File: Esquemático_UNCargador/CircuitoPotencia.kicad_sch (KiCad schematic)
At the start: 2 parts, among them J2 Neutro, J3 Conn_02x03_Counter_Clockwise

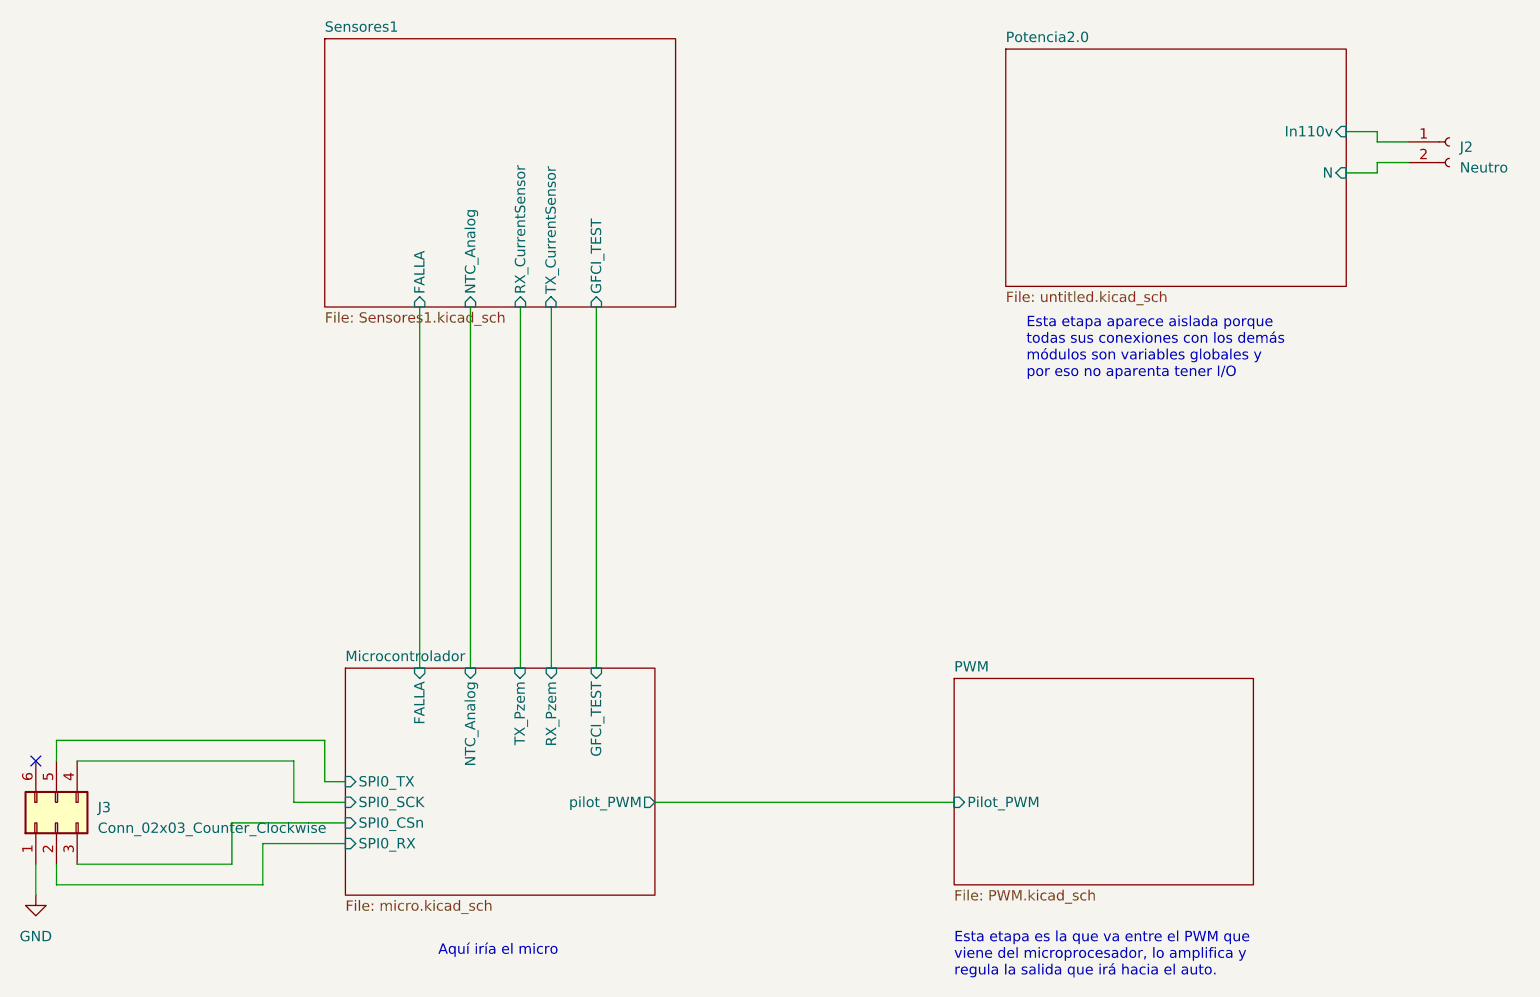
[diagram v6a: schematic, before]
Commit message: PCB con ruteo realizado. Errores en los anchos de vias -0.2mm. Huella LF356n actualizada
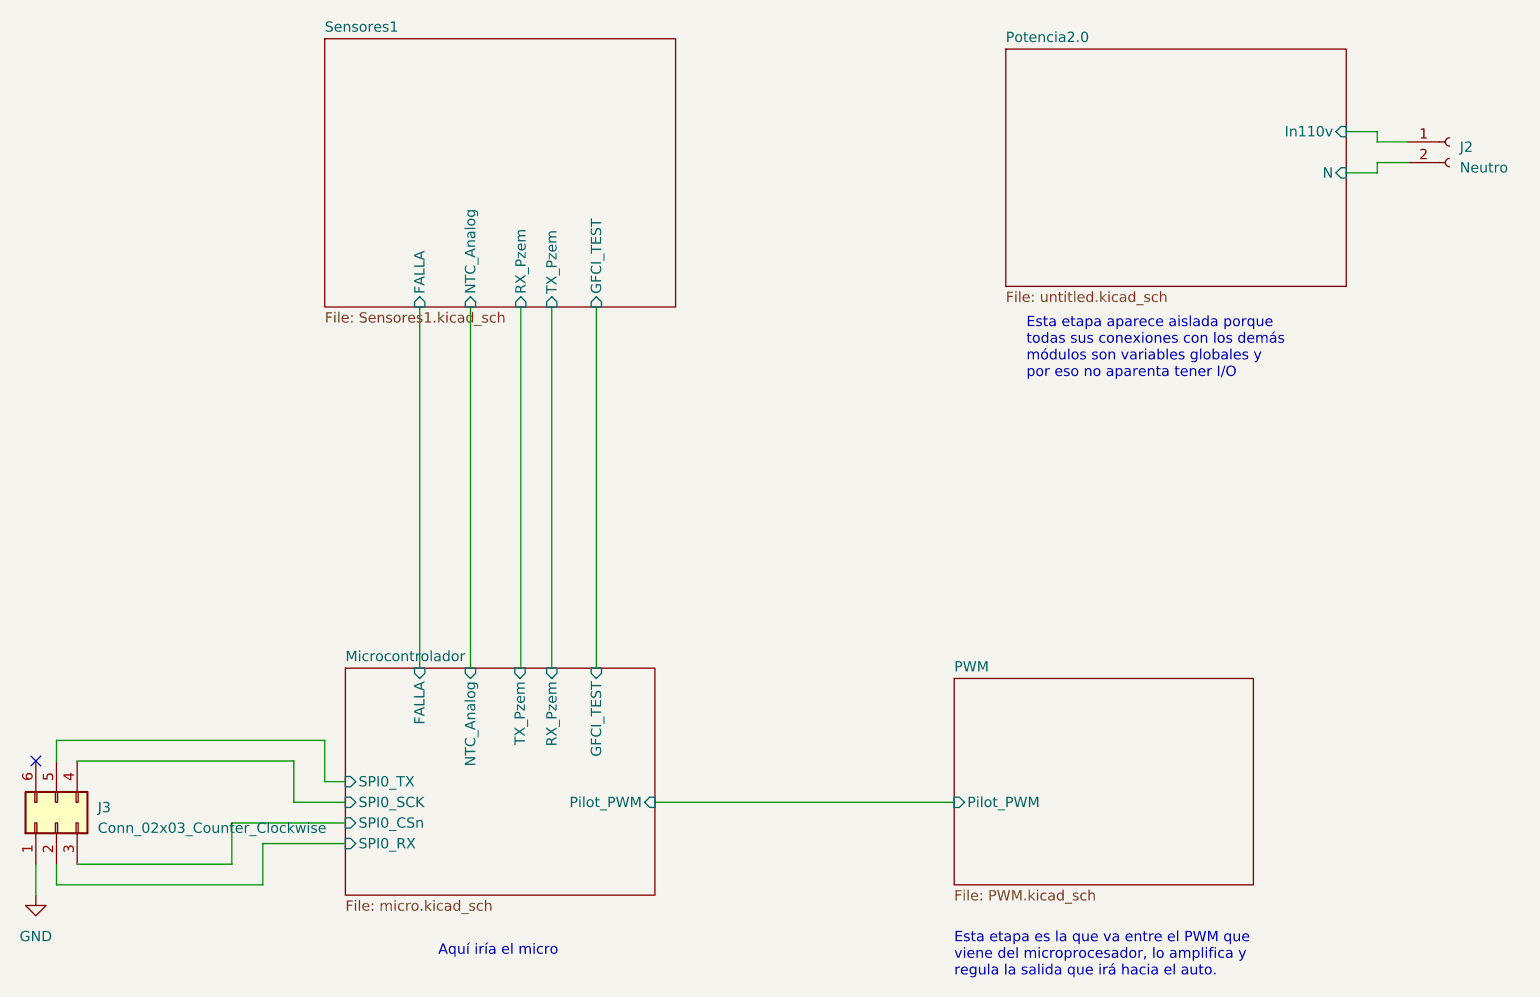
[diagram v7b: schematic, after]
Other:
- sheet Microcontrolador ports: added Pilot_PWM; removed pilot_PWM
- sheet Sensores1 ports: added RX_Pzem, TX_Pzem; removed RX_CurrentSensor, TX_CurrentSensor
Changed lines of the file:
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@@
   (paper "A4")
   (no_connect (at 20.32 129.54))
+  (wire (pts (xy 80.01 73.66) (xy 80.01 118.11))
+    (stroke (width 0) (type default))
+  )
   (wire (pts (xy 48.26 139.7) (xy 58.42 139.7))
     (stroke (width 0) (type default))
@@
     (stroke (width 0) (type default))
   )
+  (wire (pts (xy 83.82 73.66) (xy 83.82 118.11))
+    (stroke (width 0) (type default))
+  )
   (wire (pts (xy 22.86 129.54) (xy 22.86 127))
     (stroke (width 0) (type default))
@@
     (stroke (width 0) (type default))
   )
-  (wire (pts (xy 79.9592 73.66) (xy 79.9592 118.11))
-    (stroke (width 0) (type default))
-  )
   (wire (pts (xy 185.42 57.15) (xy 181.61 57.15))
     (stroke (width 0) (type default))
   )
-  (wire (pts (xy 83.7692 73.66) (xy 83.7692 118.11))
-    (stroke (width 0) (type default))
-  )
   (wire (pts (xy 52.07 129.54) (xy 25.4 129.54))
     (stroke (width 0) (type default))
@@
     (stroke (width 0) (type default))
   )
-  (wire (pts (xy 83.7692 73.66) (xy 83.7184 73.66))
-    (stroke (width 0) (type default))
-  )
   (wire (pts (xy 185.42 52.07) (xy 181.61 52.07))
     (stroke (width 0) (type default))
@@
     (stroke (width 0) (type default))
   )
-  (wire (pts (xy 79.9592 118.11) (xy 79.9084 118.11))
+  (wire (pts (xy 80.01 118.11) (xy 79.9084 118.11))
     (stroke (width 0) (type default))
   )
@@
       (effects (font (size 1.27 1.27)) (justify left top))
     )
-    (pin "pilot_PWM" output (at 96.52 134.62 0)
-      (effects (font (size 1.27 1.27)) (justify right))
-    )
     (pin "GFCI_TEST" input (at 89.3064 118.11 90)
       (effects (font (size 1.27 1.27)) (justify right))
@@
       (effects (font (size 1.27 1.27)) (justify right))
     )
-    (pin "RX_Pzem" input (at 83.7692 118.11 90)
-      (effects (font (size 1.27 1.27)) (justify right))
-    )
     (pin "SPI0_TX" input (at 58.42 132.08 180)
       (effects (font (size 1.27 1.27)) (justify left))
@@
     (pin "SPI0_RX" input (at 58.42 139.7 180)
       (effects (font (size 1.27 1.27)) (justify left))
+    )
+    (pin "Pilot_PWM" input (at 96.52 134.62 0)
+      (effects (font (size 1.27 1.27)) (justify right))
+    )
+    (pin "RX_Pzem" input (at 83.82 118.11 90)
+      (effects (font (size 1.27 1.27)) (justify right))
     )
     (instances
@@
       (effects (font (size 1.27 1.27)) (justify left))
     )
-    (pin "RX_CurrentSensor" input (at 79.9592 73.66 270)
-      (effects (font (size 1.27 1.27)) (justify left))
-    )
     (pin "GFCI_TEST" input (at 89.3064 73.66 270)
       (effects (font (size 1.27 1.27)) (justify left))
     )
-    (pin "TX_CurrentSensor" input (at 83.7184 73.66 270)
-      (effects (font (size 1.27 1.27)) (justify left))
-    )
     (pin "NTC_Analog" input (at 73.8124 73.66 270)
       (effects (font (size 1.27 1.27)) (justify left))
     )
+    (pin "TX_Pzem" input (at 83.82 73.66 270)
+      (effects (font (size 1.27 1.27)) (justify left))
+    )
+    (pin "RX_Pzem" input (at 80.01 73.66 270)
+      (effects (font (size 1.27 1.27)) (justify left))
+    )

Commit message: Cambio huella J3 embebidos
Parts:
- J3: footprint Connector_PinHeader_2.54mm:PinHeader_2x03_P2.54mm_Vertical -> Connector_IDC:IDC-Header_2x04_P2.54mm_Vertical
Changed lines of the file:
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@@
       (effects (font (size 1.27 1.27)) (justify right))
     )
-    (property "Footprint" "Connector_PinHeader_2.54mm:PinHeader_2x03_P2.54mm_Vertical" (at 22.86 137.16 0)
+    (property "Footprint" "Connector_IDC:IDC-Header_2x04_P2.54mm_Vertical" (at 22.86 137.16 0)
       (effects (font (size 1.27 1.27)) hide)
     )
